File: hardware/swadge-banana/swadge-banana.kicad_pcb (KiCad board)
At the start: 2 copper layers, 82.7 x 128.1 mm, 43 parts, among them J1 USB_B_Micro, SW1 4-1437565-2, SW2 4-1437565-2, SW3 4-1437565-2, SW4 SW_SPDT, U1 ESP-13-WROOM-02D, U2 DISP_OLED_UG-2864HSWEG01, U3 BUS_PCIexpress, U4 QMA6981, U5 AP1117-33

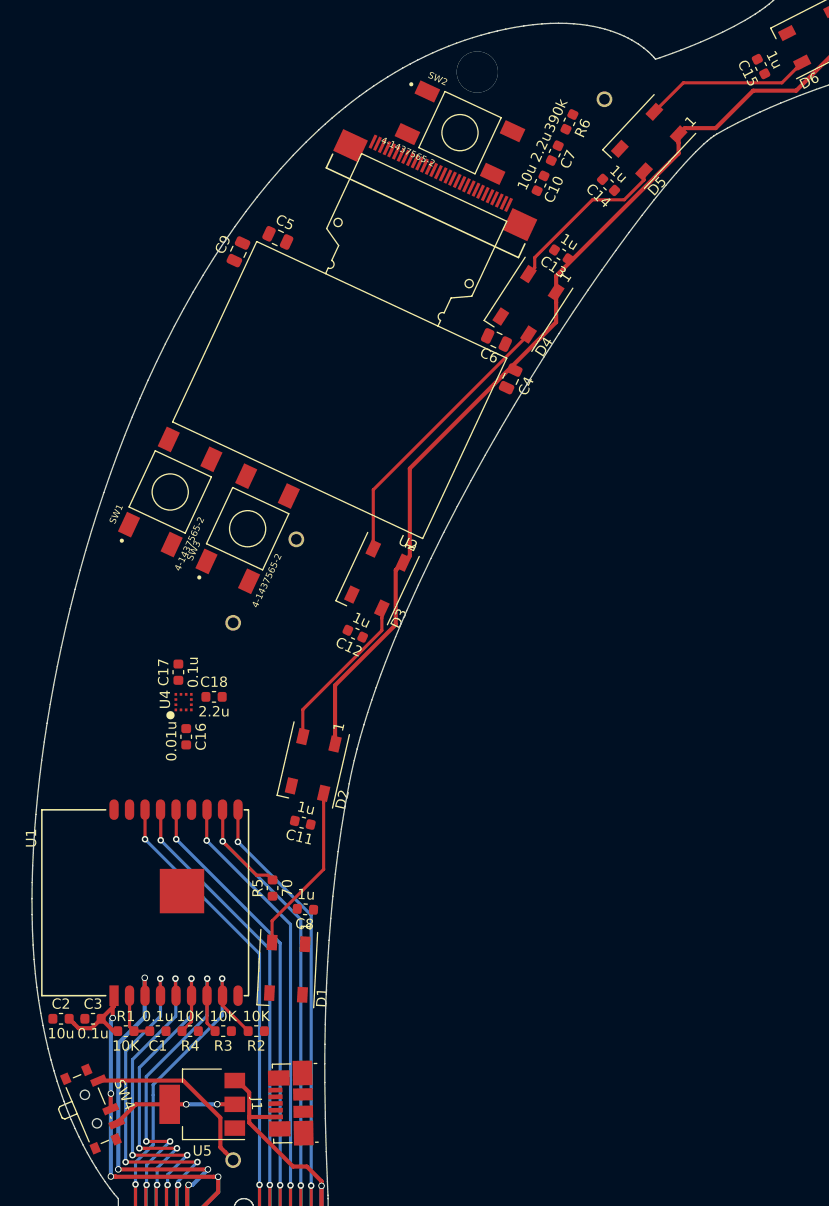
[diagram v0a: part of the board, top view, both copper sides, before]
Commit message: Fixed 3d model paths for all projects
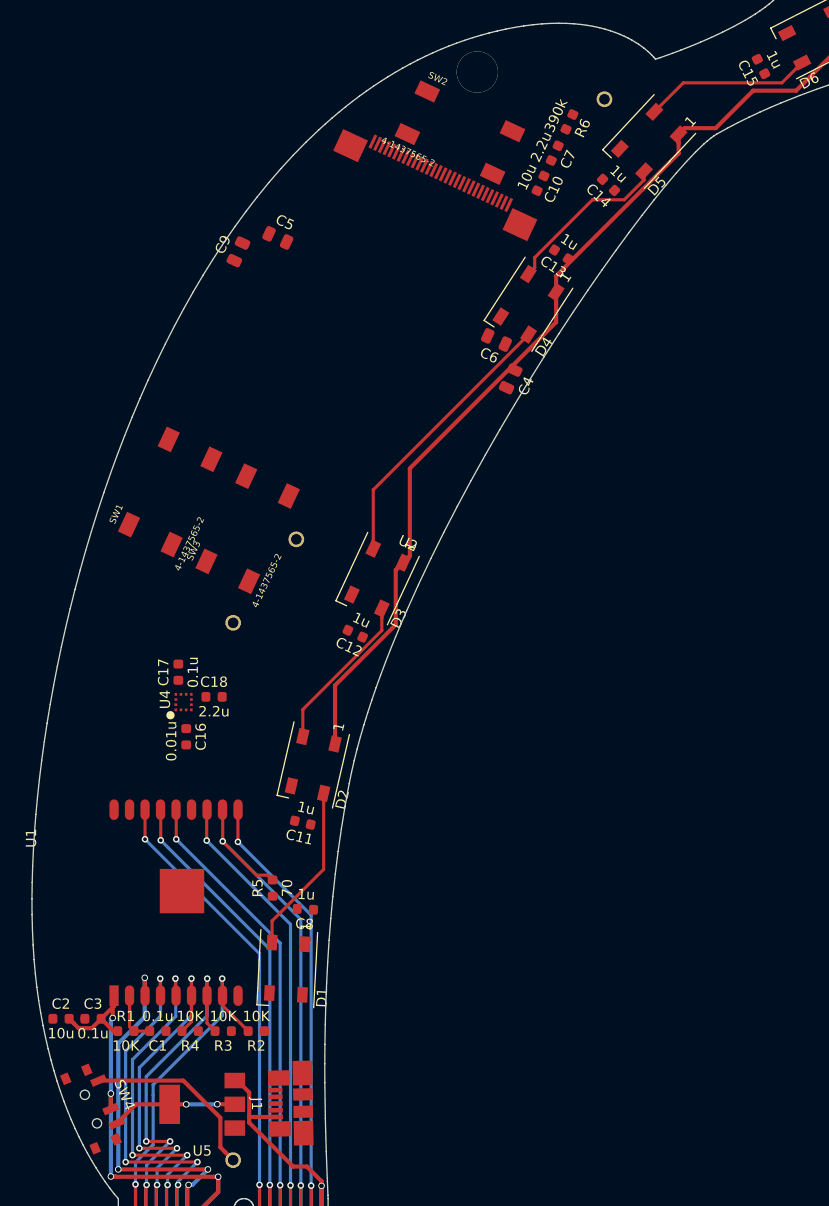
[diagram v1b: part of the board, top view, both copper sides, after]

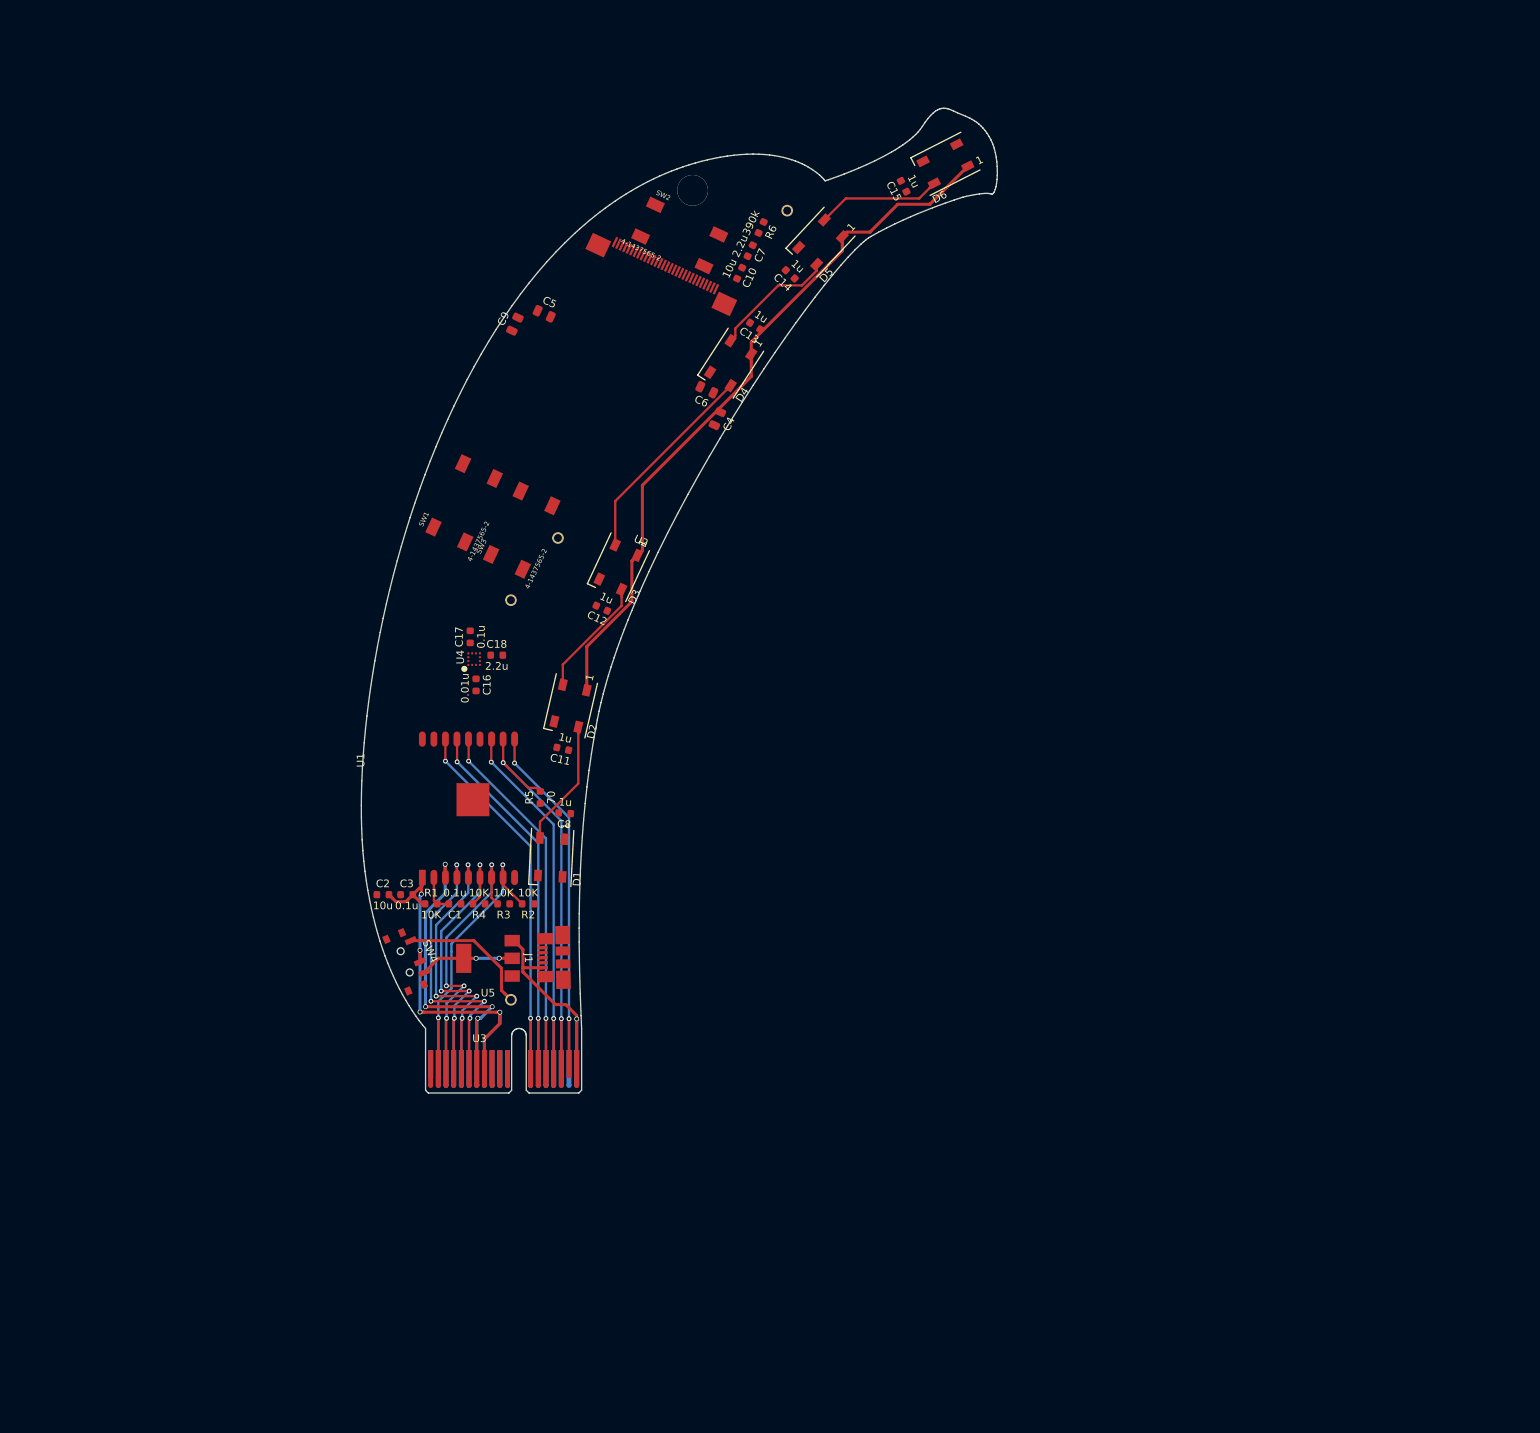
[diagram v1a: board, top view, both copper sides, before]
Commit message: Reset banana board to a blank slate for cnlohr
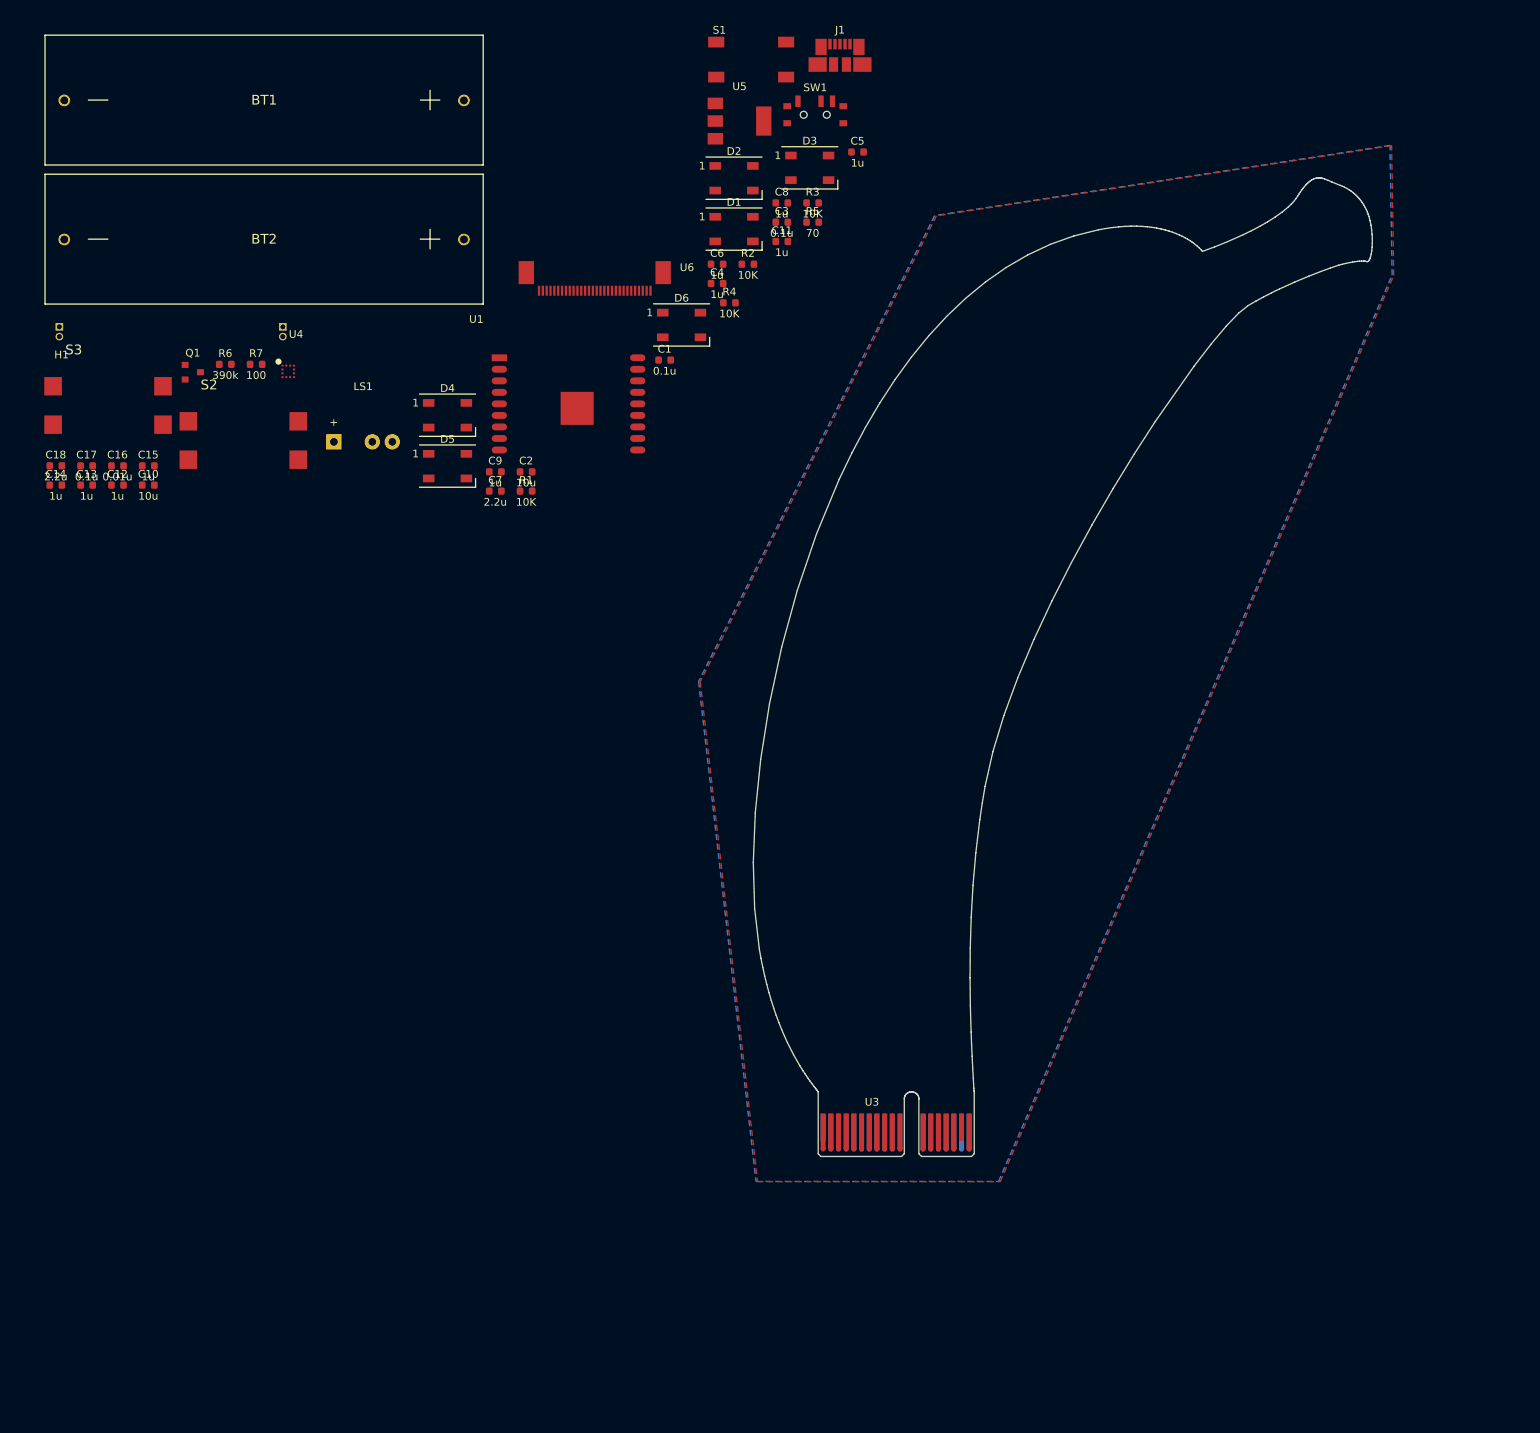
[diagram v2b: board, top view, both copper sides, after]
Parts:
- removed Ref**: Val**, Swadge_Parts:banana
- removed SW2, SW3: 4-1437565-2, Swadge_Parts:SW_4-1437565-2
- removed SW4: SW_SPDT, Swadge_Parts:SW_SPDT_PCM12
- added H1: Headband, Swadge_Parts:Headband, F.Cu at (34.8, 54.3)
- added LS1: Speaker, Swadge_Parts:Buzzer_12x9.5RM7.6, F.Cu at (56.0, 68.7)
- added Q1: Q_NPN_BEC, Swadge_Parts:SOT-23, F.Cu at (37.6, 59.6)
- added R7: 100, Swadge_Parts:R_0603_1608Metric, F.Cu at (45.8, 58.6)
- added S1: 4-1437565-2, Swadge_Parts:SW_4-1437565-2, F.Cu at (110.2, 18.9)
- added S2: B3FS-4002P, Swadge_Parts:B3FS4002P, F.Cu at (45.3, 68.5)
- added S3: B3FS-4002P, Swadge_Parts:B3FS4002P, F.Cu at (27.7, 63.9)
- added U6: OLED_CONNECTOR, Swadge_Parts:ER-OLED0.96-1.3, F.Cu at (89.9, 35.5)
- BT1, BT2: moved to F.Cu
- C4, C5, C6, C9: footprint Swadge_Parts:C_0805_2012Metric -> Swadge_Parts:C_0603_1608Metric
- SW1: value 4-1437565-2 -> SW_SPDT; footprint Swadge_Parts:SW_4-1437565-2 -> Swadge_Parts:SW_SPDT_PCM12
- U2: value DISP_OLED_UG-2864HSWEG01 -> OLED_DISPLAY; footprint Swadge_Parts:oled-flat -> Swadge_Parts:NULL
- moved J1 123.1 mm to (121.8, 18.4), turned to 0 degrees
- moved U5 113.7 mm to (108.7, 26.9), turned to 0 degrees
- moved C15 104.8 mm to (31.8, 71.8), turned to 0 degrees
- moved C3 100.2 mm to (114.2, 40.1)
- moved R3 99.6 mm to (118.2, 37.6), turned to 0 degrees
- moved C14 99.4 mm to (19.8, 74.3), turned to 0 degrees
- moved C13 89.4 mm to (23.8, 74.3), turned to 0 degrees
- moved R2 88.0 mm to (109.8, 45.5), turned to 0 degrees
- moved D1 85.1 mm to (108.0, 41.0), turned to 0 degrees
- moved R4 84.7 mm to (107.4, 50.6), turned to 0 degrees
- moved C8 84.3 mm to (114.2, 37.6), turned to 0 degrees
- moved R5 82.8 mm to (118.2, 40.1), turned to 0 degrees
- moved C10 81.7 mm to (31.8, 74.3), turned to 0 degrees
- moved BT2 79.7 mm to (46.9, 42.3), turned to 0 degrees
- moved C1 75.8 mm to (99.0, 58.0), turned to 0 degrees
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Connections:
- net SW5 renamed BZR
- D6 pad 2: Net-(D6-Pad2) -> LED_OUT
- SW1 pad 1: SW2 -> Net-(BT2-Pad1)
- SW1 pad 2: SW2 -> +3V3
- SW1 pad 3: GND -> Net-(SW1-Pad3)
- U1 pad 10: SW4 -> SW3
- U1 pad 4: SW3 -> SW1
- U3 pad A11: Net-(U3-PadA11) -> LED_OUT
- U3 pad A17: SW4 -> SW3
- U3 pad A6: SW3 -> SW1
- U3 pad B11: Net-(U3-PadB11) -> LED_OUT
- U3 pad B17: SW4 -> SW3
- U3 pad B6: SW3 -> SW1
- U5 pad 2: Net-(SW4-Pad3) -> Net-(SW1-Pad3)
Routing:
- net +3V3: track 146.3 -> 0.00 mm, vias 4 -> 0
- net RX: track 58.7 -> 0.00 mm, vias 2 -> 0
- net ADC_PIN: track 53.8 -> 0.00 mm, vias 2 -> 0
- net REST: track 53.6 -> 0.00 mm, vias 2 -> 0
- net BZR: track 53.3 -> 0.00 mm, vias 2 -> 0
- net TX: track 52.5 -> 0.00 mm, vias 2 -> 0
- net SW4: track 51.6 -> 0.00 mm, vias 2 -> 0
- net AUD_PWR: track 45.6 -> 0.00 mm, vias 4 -> 0
- net _RES: track 44.9 -> 0.00 mm, vias 4 -> 0
- net SDA: track 44.0 -> 0.00 mm, vias 4 -> 0
- net SW3: track 43.8 -> 0.00 mm, vias 4 -> 0
- net SCL: track 42.6 -> 0.00 mm, vias 2 -> 0
- net SW2: track 42.5 -> 0.00 mm, vias 4 -> 0
- net +5V: track 29.9 -> 0.00 mm, vias 1 -> 0
- net Net-(D3-Pad2): track 26.9 -> 0.00 mm
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- added copper zone on B.Cu, net GND
- added copper zone on F.Cu, net GND
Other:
- board size 82.7 x 128.1 mm -> 80.5 x 127.3 mm
- net class Default: clearance 0.19558 -> 0.2; trace_width 0.3048 -> 0.25; via_dia 0.635 -> 0.8; via_drill 0.3556 -> 0.4
- rule trace_clearance: 0.19558 -> 0.2

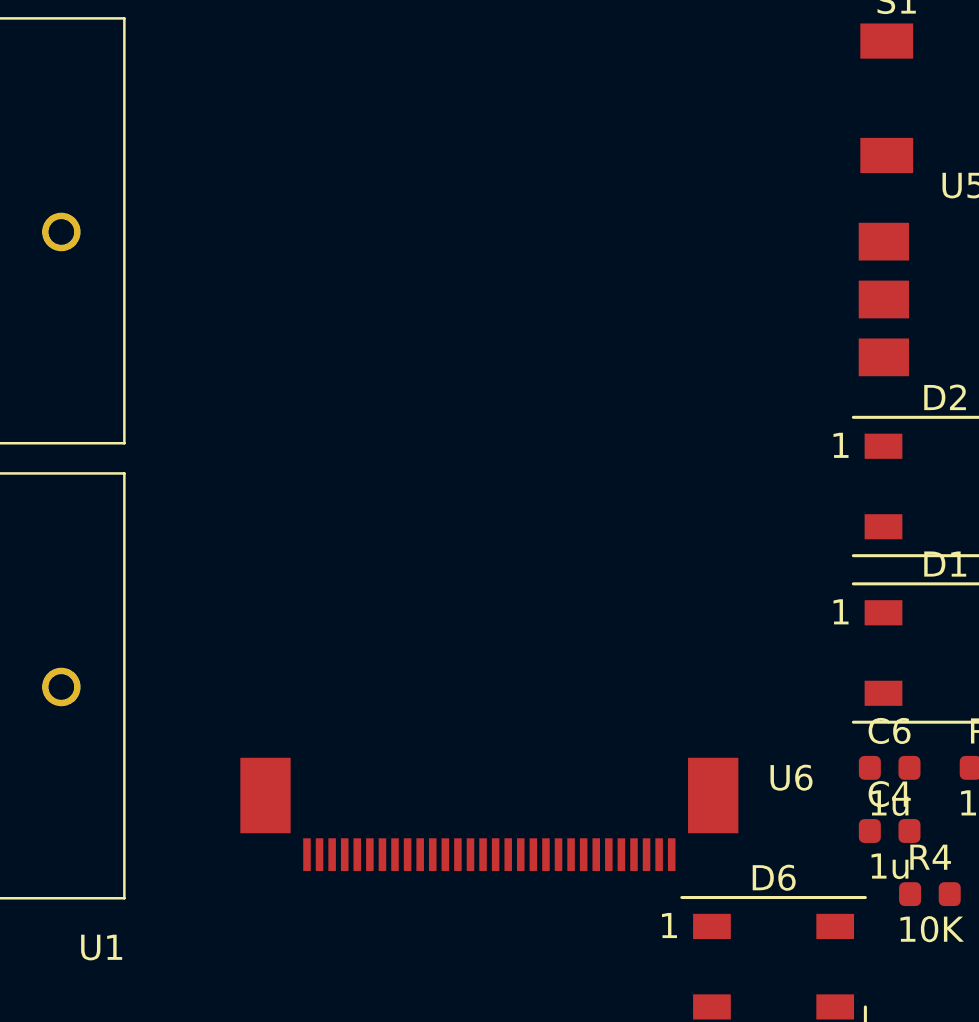
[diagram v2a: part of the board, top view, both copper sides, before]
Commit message: Changed banana OLED to wraparound
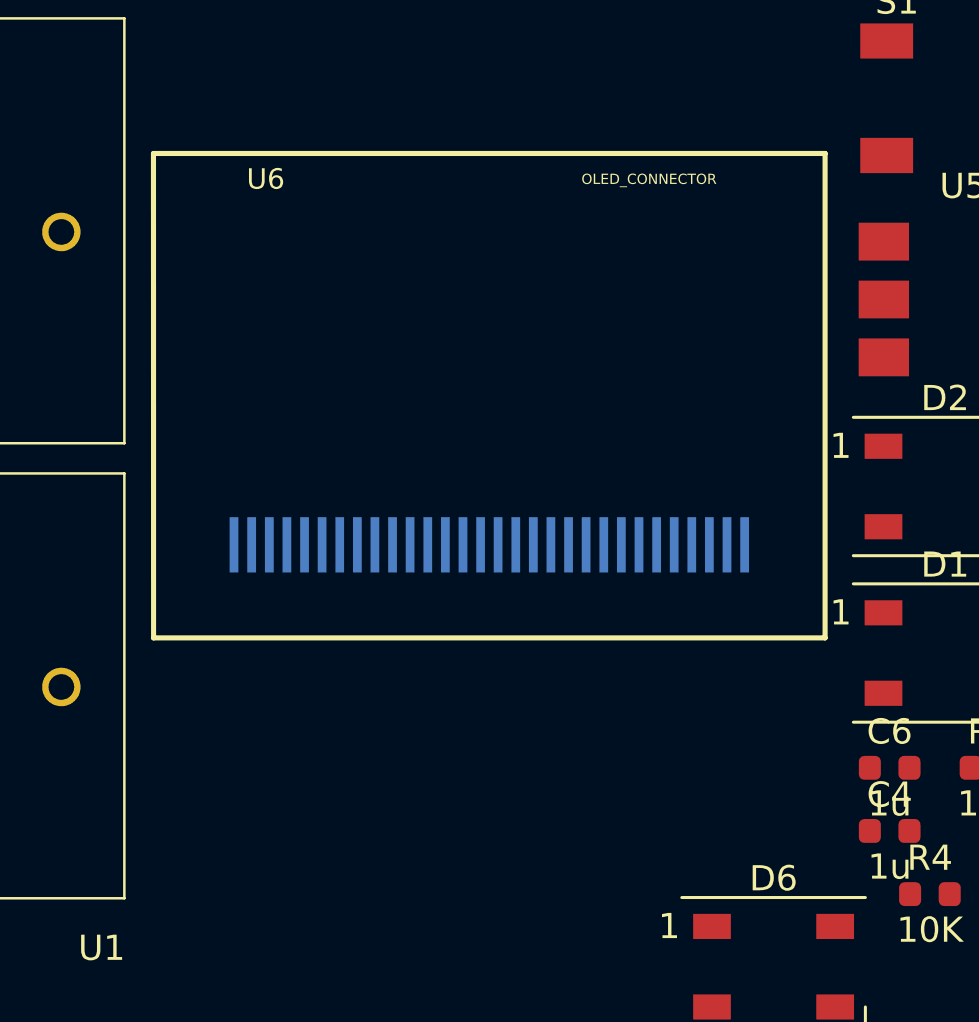
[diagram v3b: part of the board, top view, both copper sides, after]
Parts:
- removed U2: OLED_DISPLAY, Swadge_Parts:NULL
- U6: footprint Swadge_Parts:ER-OLED0.96-1.3 -> Swadge_Parts:microbuilder-UG-2864HSWEG01_0.96IN_WRAPAROUND
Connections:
- J1 pad 2: Net-(J1-Pad2) -> (no net)
- J1 pad 3: Net-(J1-Pad3) -> (no net)
- J1 pad 4: Net-(J1-Pad4) -> (no net)
- U4 pad 10: Net-(U4-Pad10) -> (no net)
- U4 pad 11: Net-(U4-Pad11) -> (no net)
- U4 pad 5: Net-(U4-Pad5) -> (no net)
- U4 pad 6: Net-(U4-Pad6) -> (no net)

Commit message: Bump design with some placements.
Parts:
- BT1, BT2: moved to B.Cu
- moved C15 153.2 mm to (182.6, 44.8), turned to 210 degrees
- moved BT1 129.0 mm to (127.2, 125.2), turned to 96 degrees
- moved S3 117.3 mm to (144.8, 70.2), turned to 60 degrees
- moved C8 113.4 mm to (121.5, 150.7), turned to 280 degrees
- moved Q1 103.4 mm to (120.2, 121.8), turned to 134 degrees
- moved BT2 103.2 mm to (146.9, 67.4), turned to 50 degrees
- moved R3 101.9 mm to (136.9, 137.7), turned to 90 degrees
- moved U1 101.4 mm to (123.8, 147.9), turned to 108 degrees
- moved R7 101.4 mm to (122.0, 125.6), turned to 300 degrees
- moved C10 100.9 mm to (127.8, 105.3)
- moved R4 100.3 mm to (131.6, 147.9), turned to 20 degrees
- moved S2 96.9 mm to (130.4, 114.8), turned to 86 degrees
- moved R6 96.4 mm to (125.0, 107.3)
- moved C1 95.7 mm to (128.0, 149.2), turned to 20 degrees
- moved D5 93.2 mm to (159.6, 43.8), turned to 180 degrees
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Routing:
- net GND: track 0.00 -> 8.78 mm
